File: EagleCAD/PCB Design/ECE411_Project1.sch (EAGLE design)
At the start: 39 parts, among them J1 0473460001_USBMICRO, U1 ATS160SM-1, U2 MIC29310-5.0WU, U3 NCP5501DT50RKG, U4 DCJACK_2.1MM_PTH

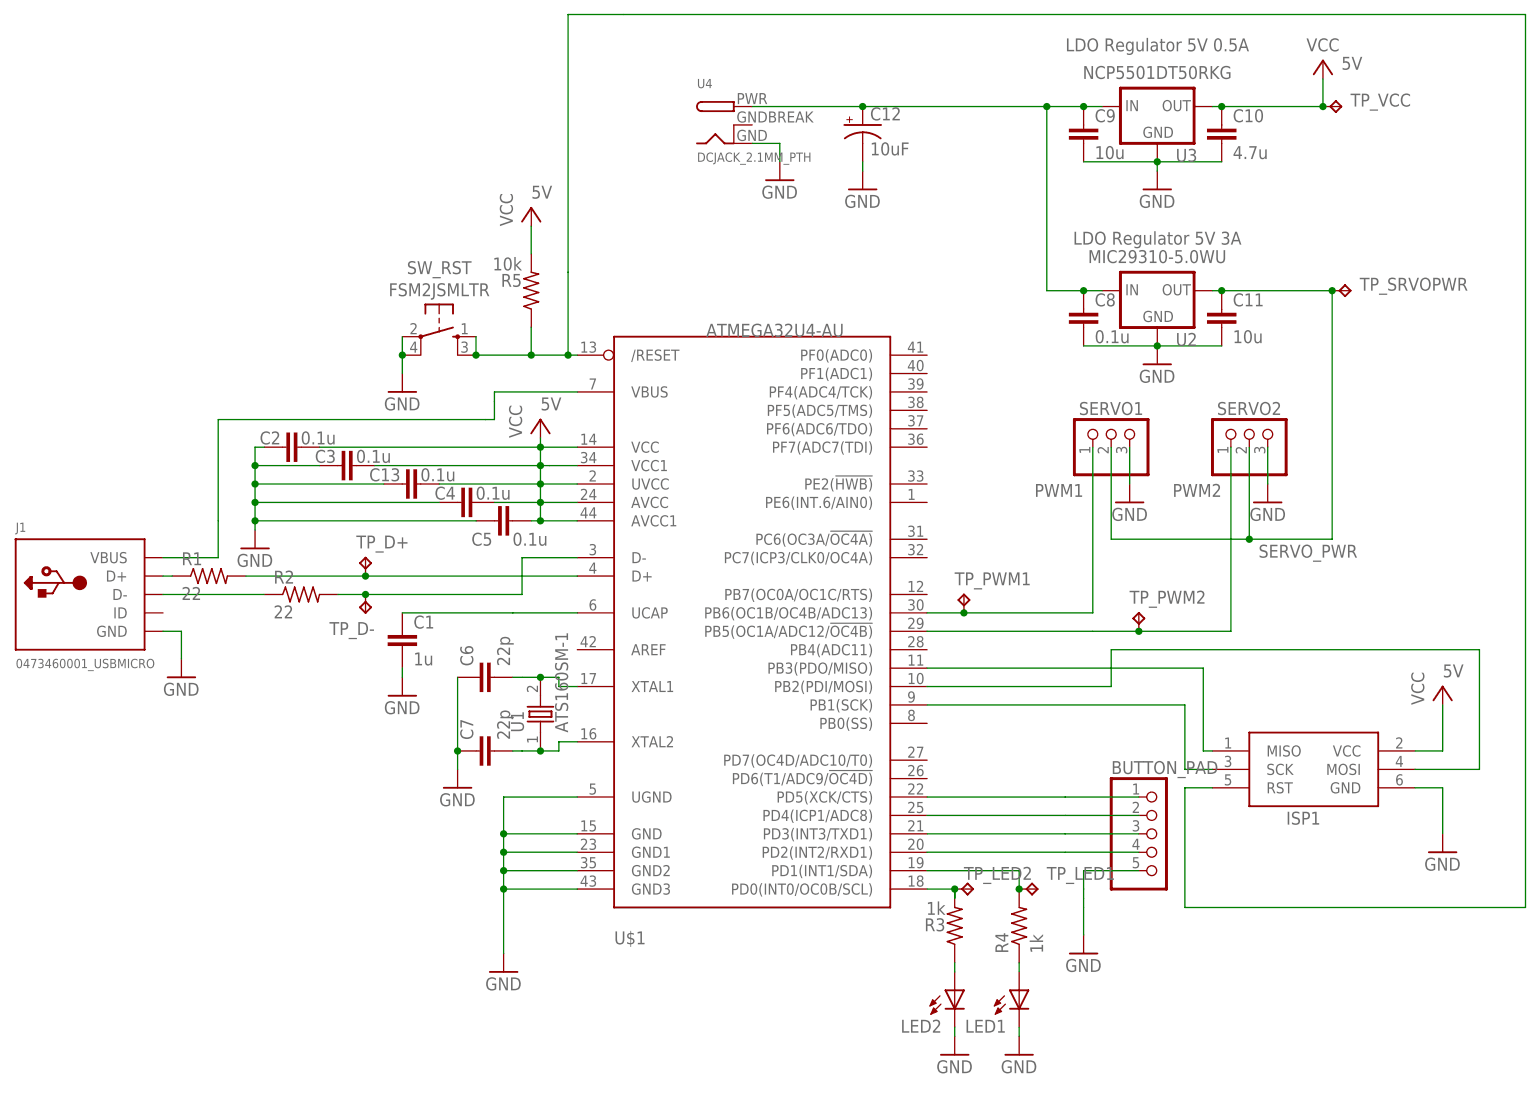
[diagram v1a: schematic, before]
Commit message: updated BOM, completed Layout. Still need to add team number and project description to schematic
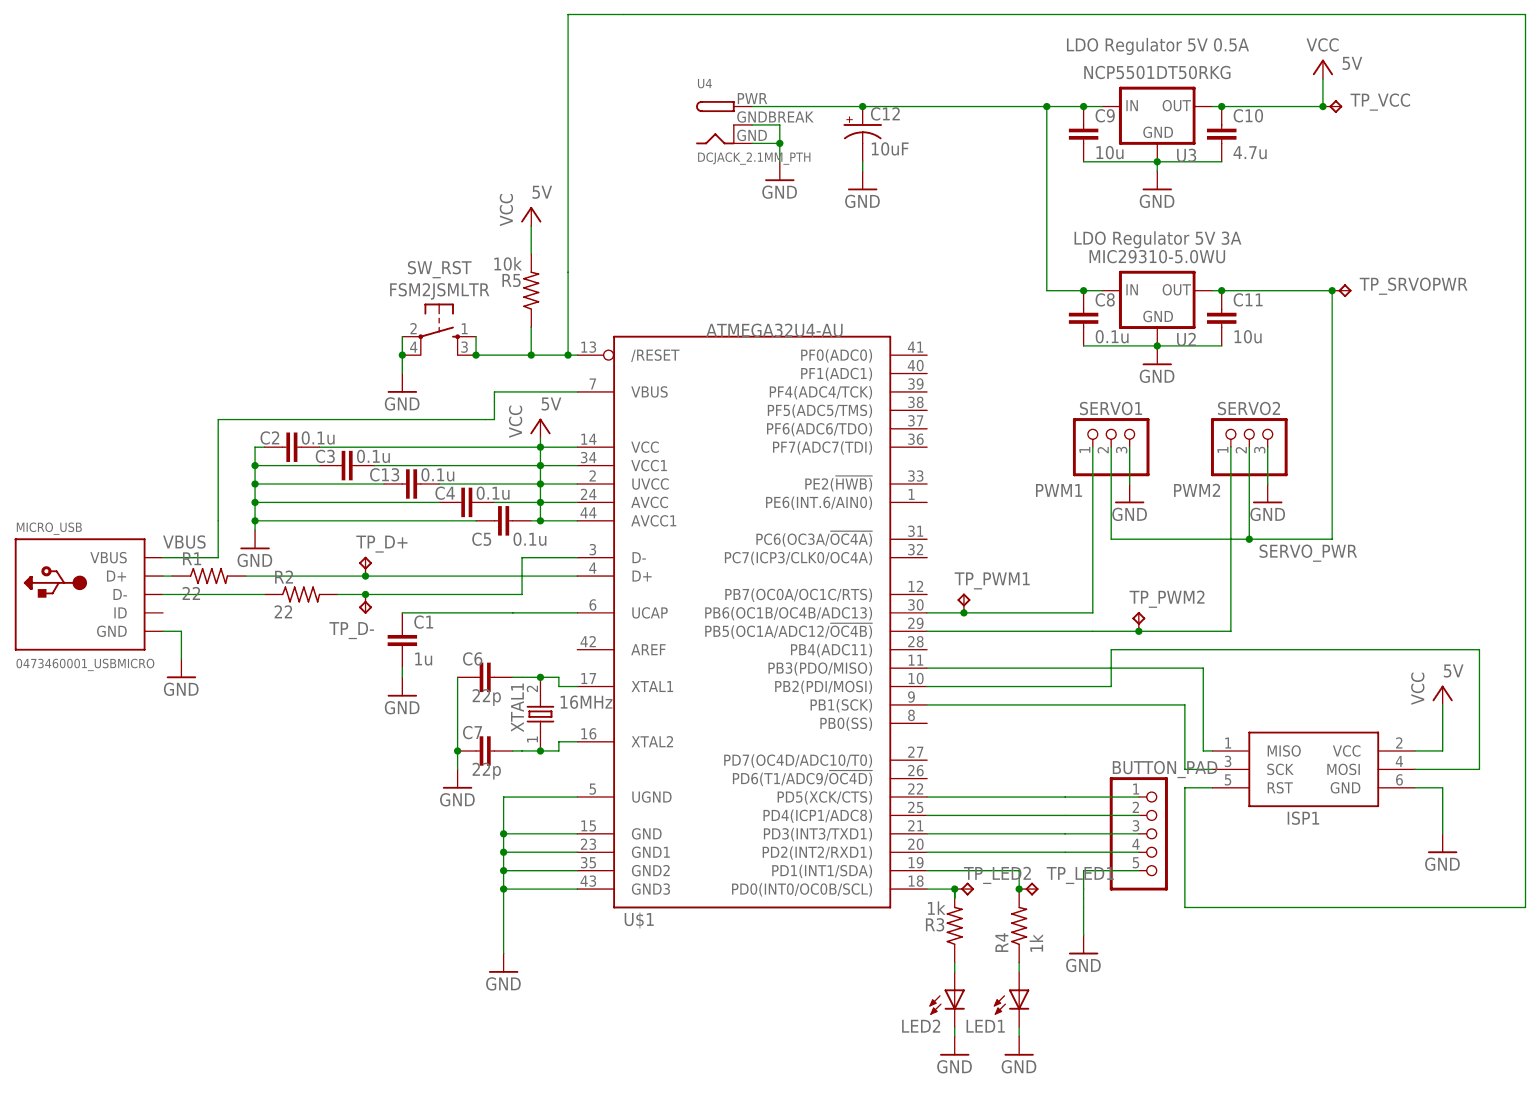
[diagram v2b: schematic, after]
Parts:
- XTAL1: value ATS160SM-1 -> 16MHz
- renumbered J1 to MICRO_USB, U1 to XTAL1
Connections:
- net N$1 renamed VBUS
- net GND: now also U4.GNDBREAK
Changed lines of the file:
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@@
 </part>
 <part name="SW_RST" library="Push_Button" deviceset="FSM2JSMLTR" device=""/>
-<part name="J1" library="USB_Micro_and_AVRISP" deviceset="0473460001_USBMICRO" device=""/>
+<part name="MICRO_USB" library="USB_Micro_and_AVRISP" deviceset="0473460001_USBMICRO" device=""/>
 <part name="ISP1" library="USB_Micro_and_AVRISP" deviceset="AVRISP" device="-6"/>
-<part name="U1" library="Xtals" deviceset="ATS160SM-1" device=""/>
+<part name="XTAL1" library="Xtals" deviceset="ATS160SM-1" device="" value="16MHz"/>
 <part name="U2" library="Regulators" deviceset="MIC29310-5.0WU" device=""/>
 <part name="U3" library="Regulators" deviceset="NCP5501DT50RKG" device=""/>
@@
 <instances>
 <instance part="U$1" gate="G$1" x="1.27" y="40.64" smashed="yes">
-<attribute name="NAME" x="-16.51" y="2.54" size="1.778" layer="95"/>
+<attribute name="NAME" x="-15.24" y="5.08" size="1.778" layer="95"/>
 <attribute name="VALUE" x="-3.81" y="86.36" size="1.778" layer="96"/>
 </instance>
@@
 <attribute name="VALUE" x="-40.64" y="93.726" size="1.778" layer="96" font="vector" align="top-center"/>
 </instance>
-<instance part="J1" gate="G$1" x="-88.9" y="50.8" smashed="yes">
+<instance part="MICRO_USB" gate="G$1" x="-88.9" y="50.8" smashed="yes">
 <attribute name="NAME" x="-99.06" y="59.436" size="1.27" layer="95"/>
 <attribute name="VALUE" x="-99.06" y="40.64" size="1.27" layer="96"/>
@@
 <attribute name="NAME" x="76.2" y="19.05" size="1.778" layer="95"/>
 </instance>
-<instance part="U1" gate="G$1" x="-26.67" y="34.29" smashed="yes" rot="R90">
+<instance part="XTAL1" gate="G$1" x="-26.67" y="34.29" smashed="yes" rot="R90">
 <attribute name="NAME" x="-28.956" y="31.75" size="1.778" layer="95" rot="R90"/>
-<attribute name="VALUE" x="-22.86" y="31.75" size="1.778" layer="96" rot="R90"/>
+<attribute name="VALUE" x="-24.13" y="36.83" size="1.778" layer="96" rot="R180" align="bottom-right"/>
 </instance>
 <instance part="U2" gate="G$1" x="58.42" y="92.71" smashed="yes">
@@
 </instance>
 <instance part="C6" gate="G$1" x="-35.56" y="39.37" smashed="yes" rot="R90">
-<attribute name="NAME" x="-35.941" y="40.894" size="1.778" layer="95" rot="R90"/>
-<attribute name="VALUE" x="-30.861" y="40.894" size="1.778" layer="96" rot="R90"/>
+<attribute name="NAME" x="-34.544" y="42.799" size="1.778" layer="95" rot="R180"/>
+<attribute name="VALUE" x="-32.004" y="37.719" size="1.778" layer="96" rot="R180"/>
 </instance>
 <instance part="C7" gate="G$1" x="-35.56" y="29.21" smashed="yes" rot="R90">
-<attribute name="NAME" x="-35.941" y="30.734" size="1.778" layer="95" rot="R90"/>
-<attribute name="VALUE" x="-30.861" y="30.734" size="1.778" layer="96" rot="R90"/>
+<attribute name="NAME" x="-34.544" y="32.639" size="1.778" layer="95" rot="R180"/>
+<attribute name="VALUE" x="-32.004" y="27.559" size="1.778" layer="96" rot="R180"/>
 </instance>
 <instance part="U4" gate="G$1" x="0" y="115.57" smashed="yes">
@@
 <wire x1="-76.2" y1="45.72" x2="-76.2" y2="41.91" width="0.1524" layer="91"/>
 <pinref part="GND12" gate="1" pin="GND"/>
-<pinref part="J1" gate="G$1" pin="GND"/>
+<pinref part="MICRO_USB" gate="G$1" pin="GND"/>
 </segment>
 <segment>
@@
 <pinref part="GND15" gate="1" pin="GND"/>
 <pinref part="U4" gate="G$1" pin="GND"/>
+<pinref part="U4" gate="G$1" pin="GNDBREAK"/>
+<wire x1="2.54" y1="115.57" x2="6.35" y2="115.57" width="0.1524" layer="91"/>
+<wire x1="6.35" y1="115.57" x2="6.35" y2="113.03" width="0.1524" layer="91"/>
+<junction x="6.35" y="113.03"/>
 </segment>
 <segment>
@@
 <wire x1="-77.47" y1="53.34" x2="-78.74" y2="53.34" width="0.1524" layer="91"/>
 <pinref part="R1" gate="G$1" pin="1"/>
-<pinref part="J1" gate="G$1" pin="D+"/>
+<pinref part="MICRO_USB" gate="G$1" pin="D+"/>
 </segment>
 </net>
@@
 <wire x1="-78.74" y1="50.8" x2="-64.77" y2="50.8" width="0.1524" layer="91"/>
 <pinref part="R2" gate="G$1" pin="1"/>
-<pinref part="J1" gate="G$1" pin="D-"/>
+<pinref part="MICRO_USB" gate="G$1" pin="D-"/>
 </segment>
 </net>
@@
 <wire x1="-21.59" y1="30.48" x2="-24.13" y2="30.48" width="0.1524" layer="91"/>
 <wire x1="-24.13" y1="30.48" x2="-24.13" y2="29.21" width="0.1524" layer="91"/>
-<pinref part="U1" gate="G$1" pin="1"/>
+<pinref part="XTAL1" gate="G$1" pin="1"/>
 <junction x="-26.67" y="29.21"/>
 <pinref part="C7" gate="G$1" pin="2"/>
@@
 <wire x1="-21.59" y1="38.1" x2="-24.13" y2="38.1" width="0.1524" layer="91"/>
 <wire x1="-24.13" y1="38.1" x2="-24.13" y2="39.37" width="0.1524" layer="91"/>
-<pinref part="U1" gate="G$1" pin="2"/>
+<pinref part="XTAL1" gate="G$1" pin="2"/>
 <junction x="-26.67" y="39.37"/>
 <pinref part="C6" gate="G$1" pin="2"/>
@@
 </segment>
 </net>
-<net name="N$1" class="0">
-<segment>
-<pinref part="J1" gate="G$1" pin="VBUS"/>
+<net name="VBUS" class="0">
+<segment>
+<pinref part="MICRO_USB" gate="G$1" pin="VBUS"/>
 <wire x1="-78.74" y1="55.88" x2="-71.12" y2="55.88" width="0.1524" layer="91"/>
 <wire x1="-71.12" y1="55.88" x2="-71.12" y2="60.96" width="0.1524" layer="91"/>
@@
 <wire x1="-33.02" y1="77.47" x2="-33.02" y2="78.74" width="0.1524" layer="91"/>
 <wire x1="-33.02" y1="78.74" x2="-21.59" y2="78.74" width="0.1524" layer="91"/>
-</segment>
-</net>
+<label x="-78.74" y="57.15" size="1.778" layer="95"/>
+</segment>
+</net>

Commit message: added name and project description to schematic
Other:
- note added: "ECE411 Team 14 Servo-Powered Pan & Tilt Camera Mount"
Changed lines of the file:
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@@
 <layer number="104" name="Name" color="7" fill="1" visible="no" active="yes"/>
 <layer number="105" name="Beschreib" color="9" fill="1" visible="no" active="yes"/>
-<layer number="106" name="BGA-Top" color="4" fill="1" visible="no" active="yes"/>
+<layer number="106" name="BGA-Top" color="4" fill="1" visible="yes" active="yes"/>
 <layer number="107" name="BD-Top" color="5" fill="1" visible="no" active="yes"/>
 <layer number="108" name="fp8" color="7" fill="1" visible="no" active="yes"/>
@@
 <text x="58.42" y="125.73" size="1.778" layer="96" align="bottom-center">LDO Regulator 5V 0.5A</text>
 <text x="58.42" y="99.06" size="1.778" layer="96" align="bottom-center">LDO Regulator 5V 3A</text>
+<text x="54.61" y="-24.13" size="3.81" layer="106">ECE411 Team 14
+Servo-Powered Pan &amp; Tilt Camera Mount</text>
 </plain>
 <instances>
@@
 </drawing>
 <compatibility>
+<note version="6.3" minversion="6.2.2" severity="warning">
+Since Version 6.2.2 text objects can contain more than one line,
+which will not be processed correctly with this version.
+</note>
 <note version="8.2" severity="warning">
 Since Version 8.2, EAGLE supports online libraries. The ids
